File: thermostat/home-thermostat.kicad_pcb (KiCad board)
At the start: 4 copper layers, 98.6 x 50.2 mm, 135 parts, among them J1 Amphenol_132289 SMA, J2 Conn_01x24, J3 Thermosthat - Molex PicoBlade, J4 Conn_ARM_JTAG_SWD_10, J5 Conn_01x20, J6 Conn_02x02_Odd_Even, J7 UART, Q1 BSS806NL6327, Q2 BSS806NL6327, Q3 BSS806NL6327, Q4 BSS806NL6327, Q5 BSS806NL6327, Q6 BSS806NL6327, U1 MKW41Z512VHT, U10 SN74LVC2T45DCUR, U2 MCP7940N-xMS, U3 MCP9844, U4 AT24C512, U5 LM2574M-5, U6 LD1117S33TR_SOT223, U7 LM358, U8 PCF8574, U9 SN74LVC2T45DCUR, Y1 32MHz 10PPM SMT 2.0x1.6mm 10PF, Y2 32.768KHz 20PPM 3.2x1.5mm 7PF, Y3 32.768KHz 20PPM 3.2x1.5mm 7PF

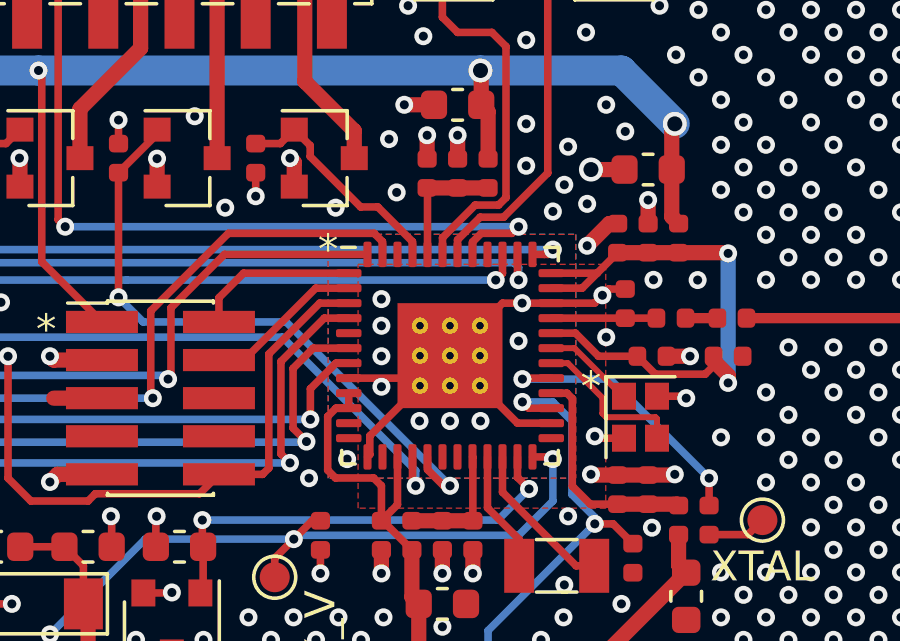
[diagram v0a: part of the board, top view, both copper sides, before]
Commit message: Changed footprint of MKW41Z to one with individual center GND pads and no thermal vias so that I am able to set own via sizes for the thermals.
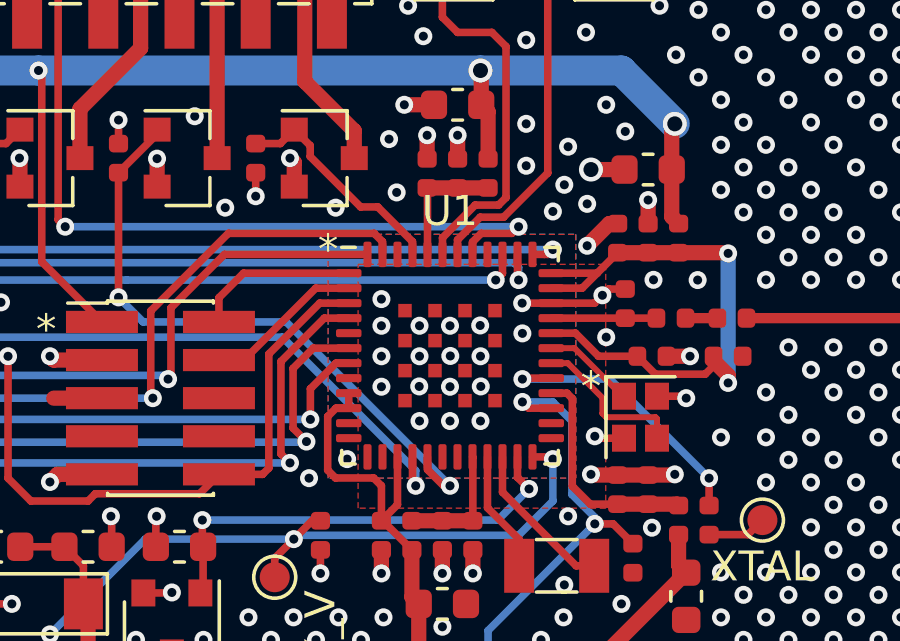
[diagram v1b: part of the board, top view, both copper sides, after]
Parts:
- U1: footprint Package_DFN_QFN:NXP_LQFN-48-1EP_7x7mm_P0.5mm_EP3.5x3.5mm_16xMask0.45x0.45_ThermalVias -> Package_DFN_QFN:NXP_LQFN-48-1EP_7x7mm_P0.5mm_EP3.5x3.5mm_16xMask0.45x0.45
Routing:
- net GND: track 145.5 -> 129.9 mm, vias 1240 -> 1249

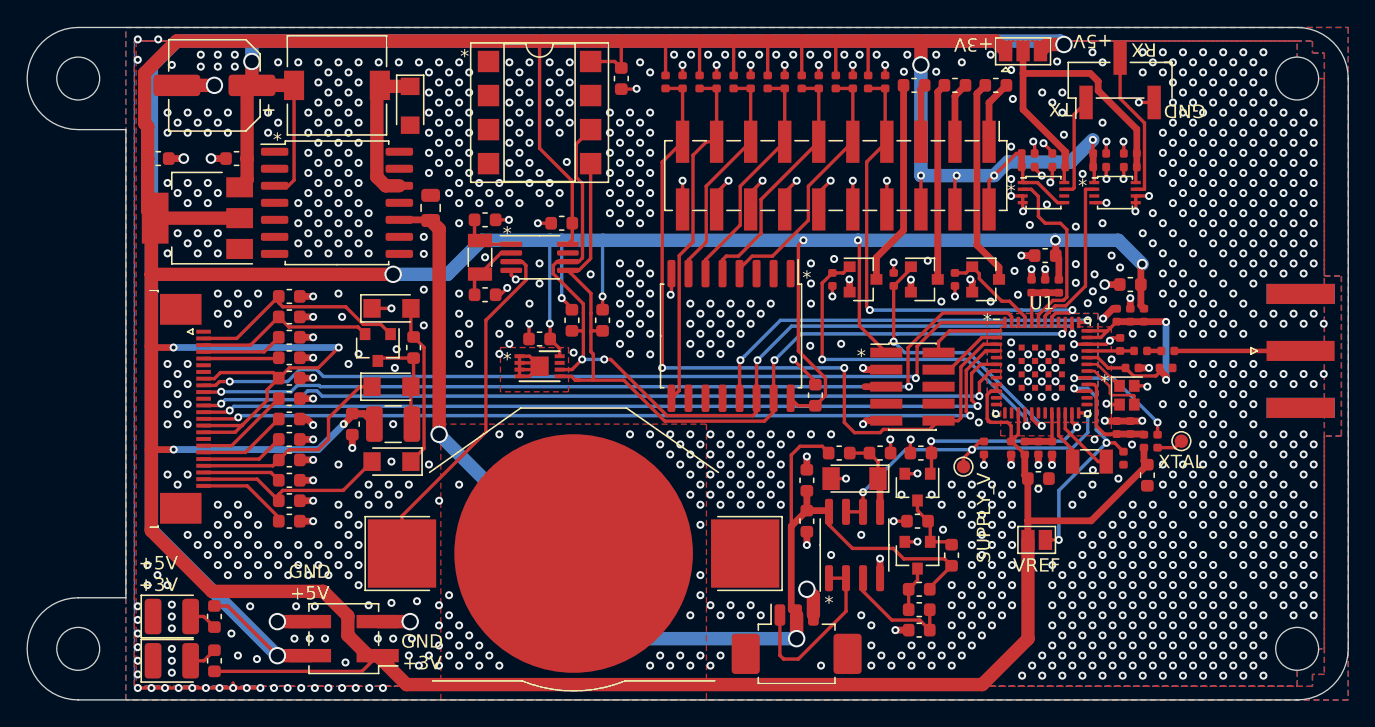
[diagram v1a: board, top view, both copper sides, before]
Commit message: Replaced DCDC input cap as the package was way too small for the required capacitance, started working on the BOM and looking up parts on Mouser. Need to replace input Molex connector as it is not in stock at Mouser. Easiest is solder pads (I will have a connector on the other side of the cable anyway...) or just the same connector but with higher pincount that Mouser has in stock
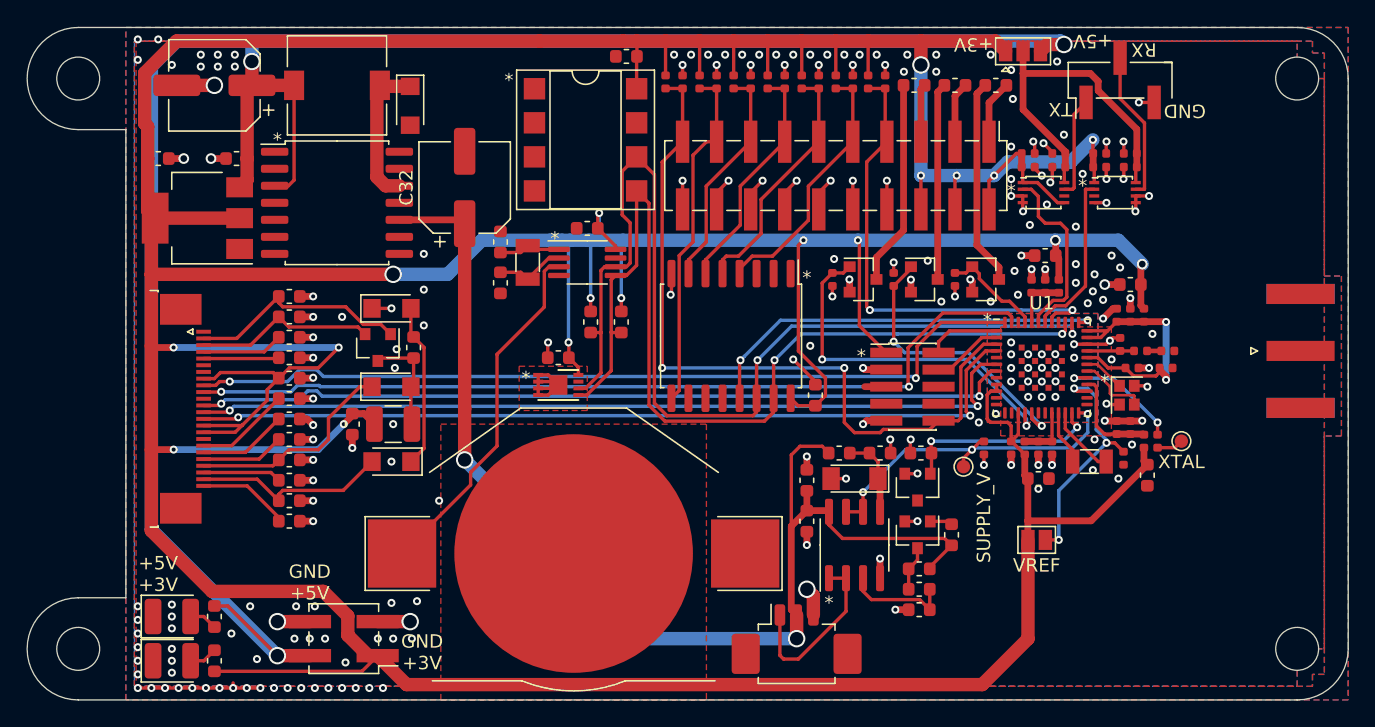
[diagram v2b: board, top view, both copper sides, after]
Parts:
- removed R26: 0, Resistor_SMD:R_0603_1608Metric
- C32: footprint Capacitor_SMD:C_0805_2012Metric -> Capacitor_SMD:CP_Elec_6.3x3
- moved U4 3.99 mm to (115.1, 82.4)
- moved U2 3.58 mm to (115.2, 91.6)
- moved Y3 3.58 mm to (110.7, 91.6)
- moved C32 2.96 mm to (106.0, 86.0)
- moved C12 2.01 mm to (108.7, 90.0), turned to 270 degrees
- moved C30 1.98 mm to (113.0, 98.7)
- moved U3 1.98 mm to (113.0, 100.7)
- moved C27 1.94 mm to (115.2, 89.0)
- moved C31 1.69 mm to (118.1, 76.2), turned to 180 degrees
- moved C37 1.52 mm to (140.0, 117.5)
- moved Q6 1.52 mm to (139.8, 111.9)
- moved R10 1.52 mm to (142.4, 111.9)
- moved R12 1.52 mm to (140.0, 116.0)
- moved R11 1.52 mm to (140.0, 114.4)
- moved C28 1.45 mm to (108.7, 93.1), turned to 90 degrees
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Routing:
- net /I2C1_SCL: track 68.1 -> 78.4 mm, vias 4 -> 2
- net +3V3: track 491.0 -> 480.8 mm, vias 17 -> 18
- net Net-(C13-Pad1): track 9.42 -> 0.00 mm
- net /I2C1_SDA: track 64.1 -> 72.2 mm
- net GND: track 129.9 -> 123.9 mm, vias 1249 -> 218
- net Net-(Q2-Pad3): track 5.15 -> 1.68 mm
- net +36V: track 87.3 -> 88.0 mm
- net Net-(C37-Pad1): track 8.68 -> 8.05 mm
- net Net-(C12-Pad2): track 4.16 -> 4.69 mm
- net Net-(C28-Pad2): track 4.70 -> 5.23 mm

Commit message: Replaced Molex PicoBlade SMT connector with THT version as this is available at Mouser. This also helps since the pins act as vias. Resolved DRC errors, Antenna trace needs to be set then we are ready for production.
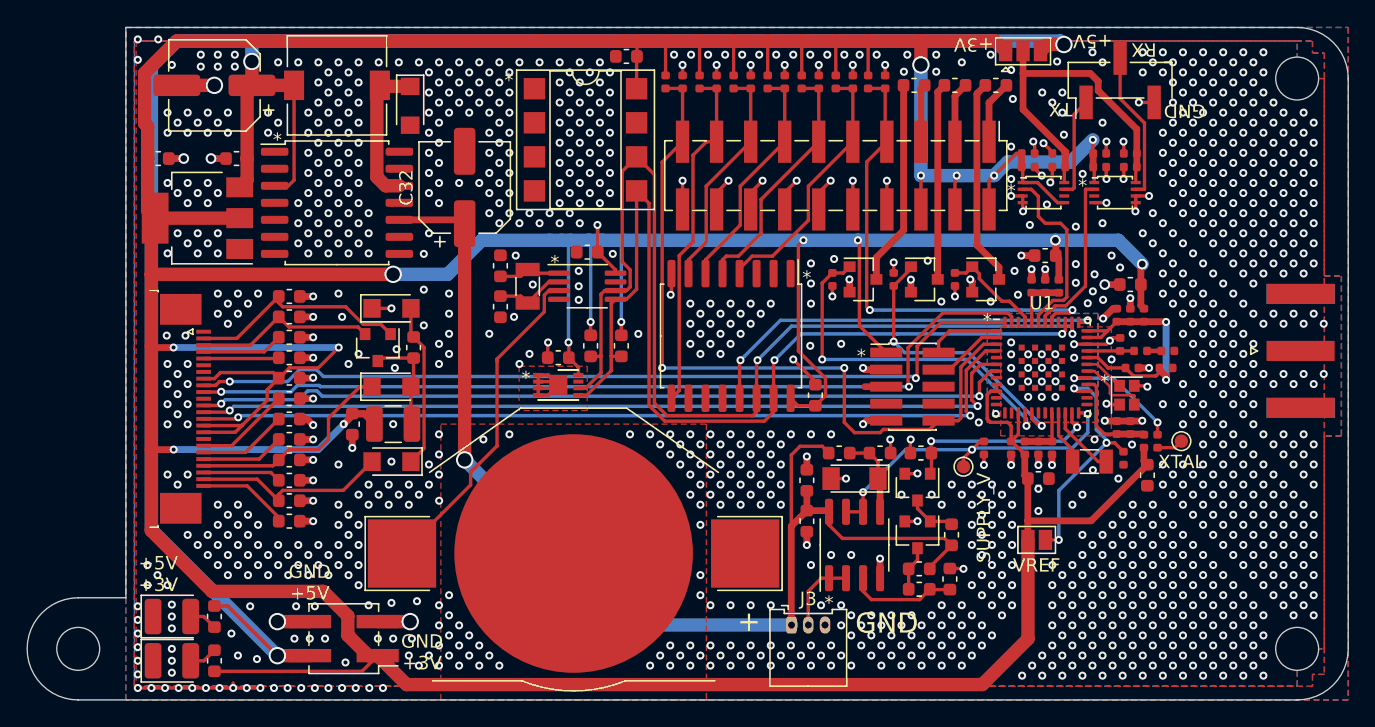
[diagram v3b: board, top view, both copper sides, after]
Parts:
- removed TP4: TestPoint, MountingHole:MountingHole_3.2mm_M3
- C12, C28: value 0 -> 5p
- J3: footprint Connector_Molex:Molex_PicoBlade_53261-0371_1x03-1MP_P1.25mm_Horizontal -> Connector_Molex:Molex_PicoBlade_53048-0310_1x03_P1.25mm_Horizontal
- moved C37 3.23 mm to (142.2, 115.2), turned to 90 degrees
- moved C27 1.78 mm to (115.2, 90.8)
- moved C28 1.78 mm to (108.7, 94.9)
- moved R5 1.78 mm to (115.4, 97.8)
- moved R6 1.78 mm to (117.7, 97.8)
- moved U2 1.78 mm to (115.2, 93.3)
- moved Y3 1.78 mm to (110.7, 93.3)
- moved C12 1.78 mm to (108.7, 91.8)
- moved J3 1.69 mm to (130.4, 118.6)
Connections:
- J3 pad 1: /regulator_out/pwm_out -> +36V
- J3 pad 2: +36V -> /regulator_out/pwm_out
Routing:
- net /regulator_out/pwm_out: track 13.3 -> 5.92 mm
- net +3V3: track 480.8 -> 484.7 mm
- net GND: track 123.9 -> 121.7 mm, vias 218 -> 1267
- net +36V: track 88.0 -> 86.1 mm, vias 2 -> 1
- net Net-(Q2-Pad3): track 1.68 -> 3.63 mm
- net Net-(BT1-Pad1): track 26.7 -> 24.9 mm
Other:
- outline, holes or cut-outs redrawn
- board text added: "+"

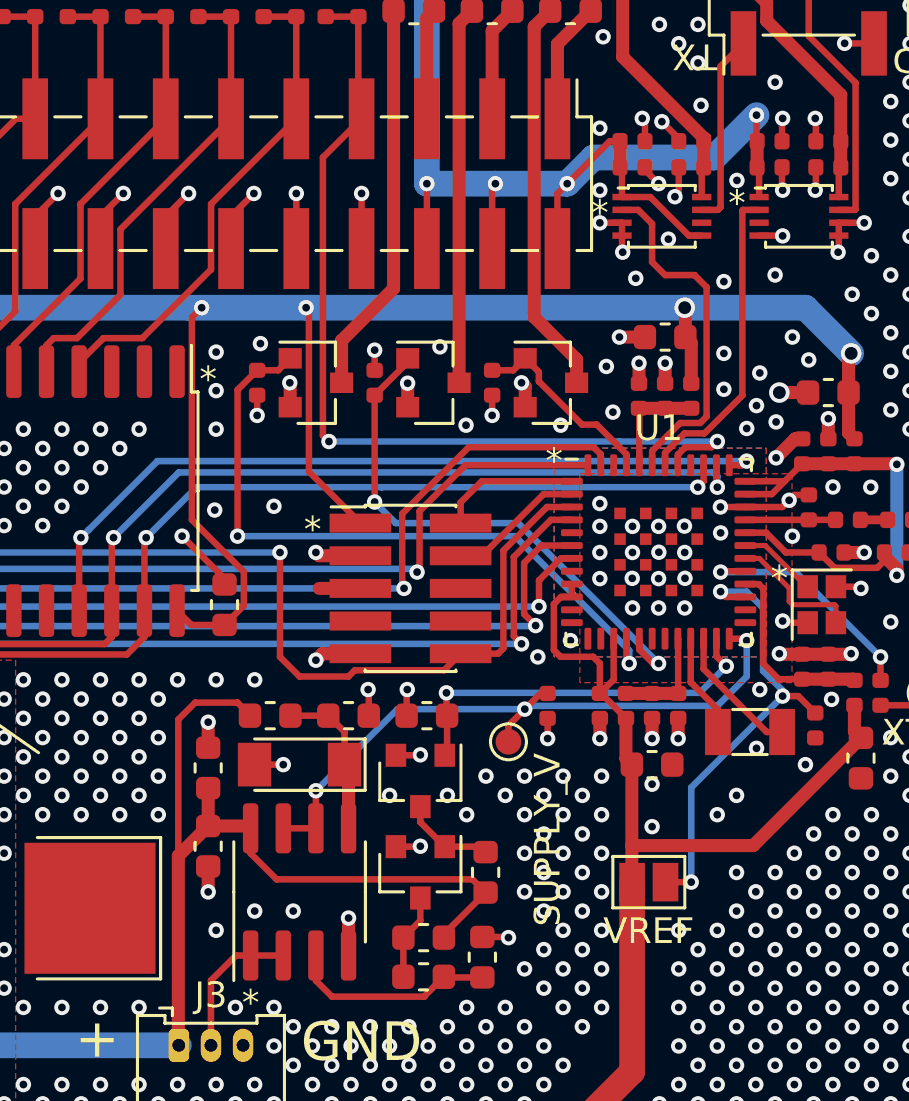
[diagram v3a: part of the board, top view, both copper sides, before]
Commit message: Changed Button lines to MKW41 pins that also have LLWU interrupt capabilities. It will never get there, but who knows what the future brings.
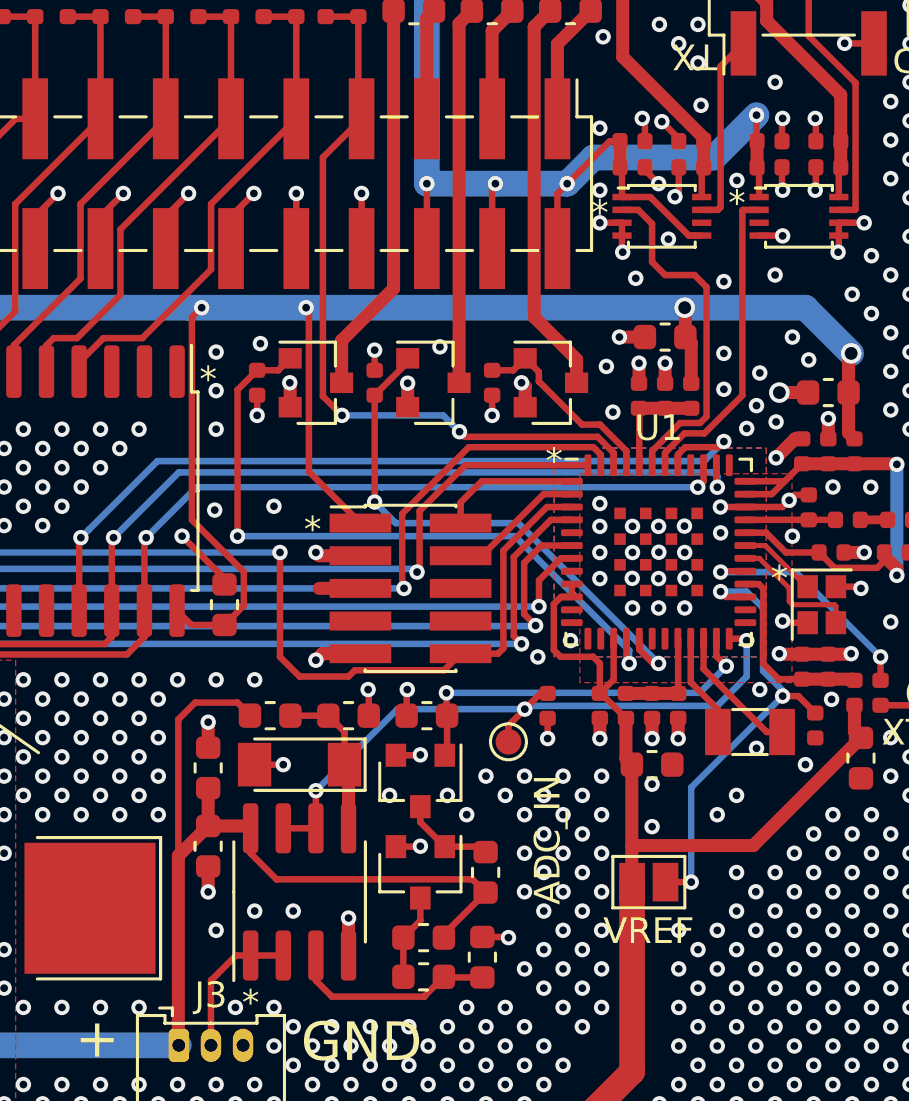
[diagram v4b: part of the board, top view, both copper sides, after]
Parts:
- TP14: value SUPPLY_V -> ADC_IN
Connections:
- U1 pad 37: /~BTN_INT -> Net-(U1-Pad37)
- U1 pad 41: /BTN_OK -> /~BTN_INT
- U1 pad 46: Net-(U1-Pad46) -> /BTN_OK
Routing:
- net /BTN_OK: track 35.8 -> 29.4 mm
- net /~BTN_INT: track 30.9 -> 31.8 mm
- net GND: vias 1267 -> 1265

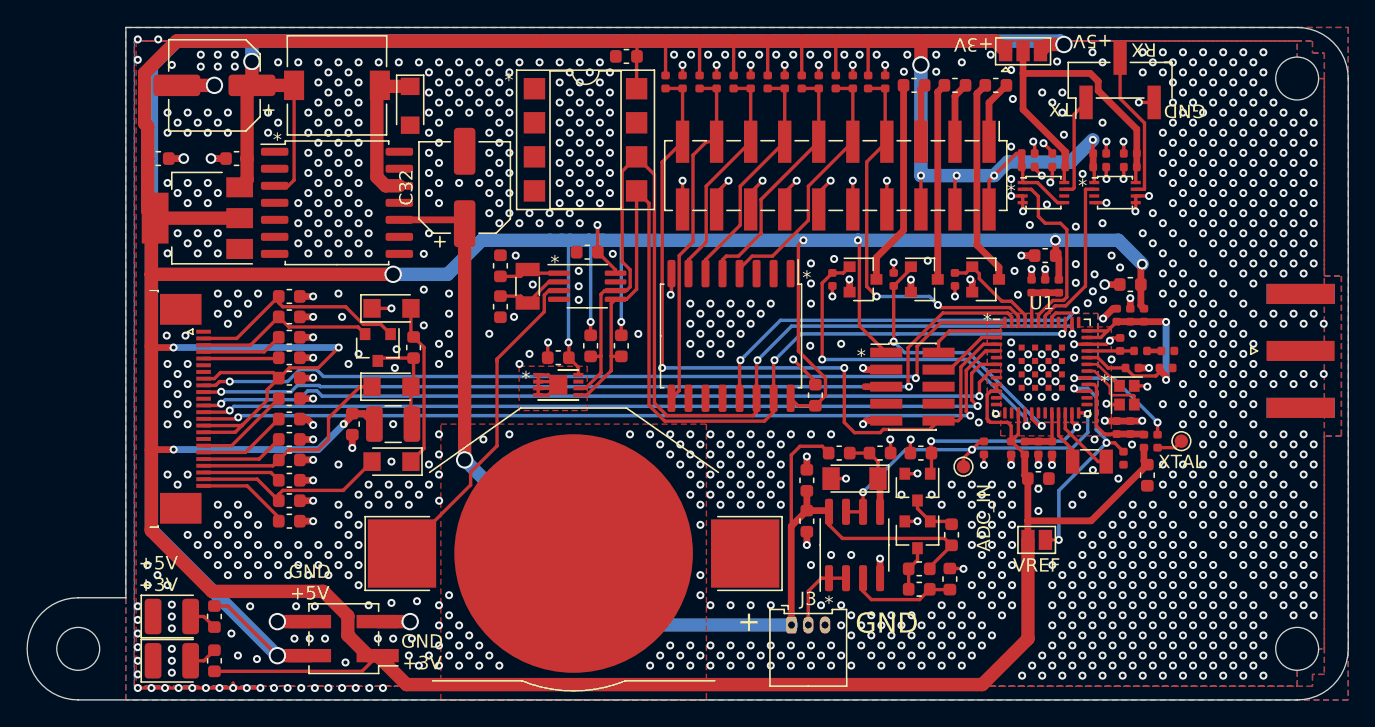
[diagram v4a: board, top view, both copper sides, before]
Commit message: Finished layouting tempsensor and thermostat. Parts are ordered from Mouser, PCB ordered from beta-layout.
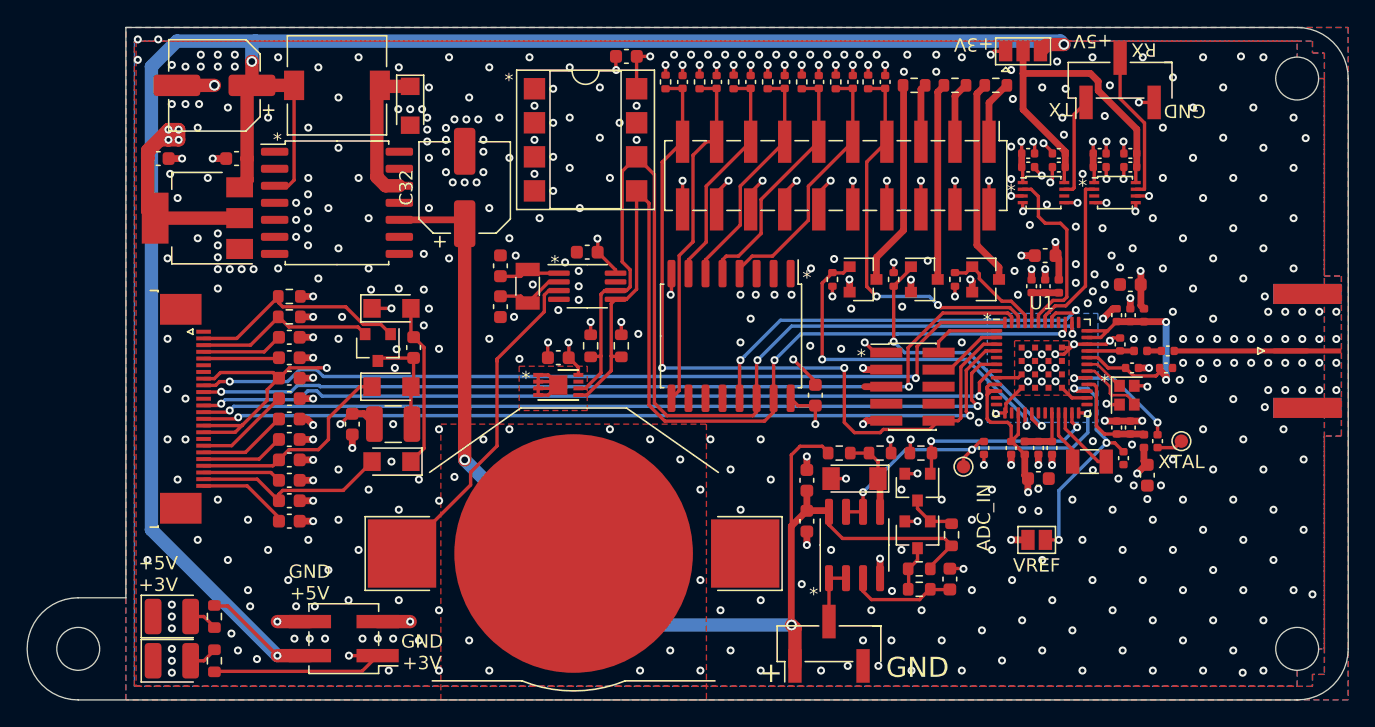
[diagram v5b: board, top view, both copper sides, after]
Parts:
- C27, C30: value 10n -> 1u
- J3: footprint Connector_Molex:Molex_PicoBlade_53048-0310_1x03_P1.25mm_Horizontal -> Connector_PinHeader_2.54mm:PinHeader_1x03_P2.54mm_Vertical_SMD_Pin1Left
- moved J3 3.12 mm to (133.2, 120.0), turned to 90 degrees
- moved J1 0.51 mm to (168.9, 98.2)
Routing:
- net +3V3: track 484.7 -> 118.9 mm, vias 18 -> 33
- net Net-(C13-Pad1): track 0.00 -> 9.93 mm
- net +36V: track 86.1 -> 89.2 mm, vias 1 -> 2
- net /regulator_out/pwm_out: track 5.92 -> 4.69 mm
- net GND: track 121.7 -> 120.8 mm, vias 1265 -> 498
- added copper zone on In2.Cu, net +3V3
- removed copper zone on In2.Cu, net GND
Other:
- net class RF added: clearance 0.2, trace_width 0.38276, via_dia 0.6, via_drill 0.3
- board text added: "MATCH CENTER PIN WIDTH TO CPW TRACE!"
